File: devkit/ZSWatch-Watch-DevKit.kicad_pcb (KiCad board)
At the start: 4 copper layers, 100 x 70 mm, 129 parts, among them IC401 nPM1300-QEXX, IC501 APDS-9306-065, IC502 BMI270, IC503 LIS2MDLTR, IC504 BMP581, IC505 DRV2603RUNT, IC506 PCA9306JK, IC507 RV-8263-C8, IC601 FAN5622SX, IC602 USBLC6-2P6, IC603 MX25U51245GZ4I00, IC604 NTS0104GU12, M601 NORA-B106, Q401 PMZ550UNEYL, Q402 PMZ550UNEYL, Q403 PMZ550UNEYL, Q404 PMZB320UPEYL, X401 Battery, X402 Battery, X403 Power, X501 Current, X502 I2S, X503 Current, X504 I2C, X505 Current, X506 Current, X507 Current, X508 Current, X509 Motor, X510 Current, X601 DEBUG, X602 Current, X603 Device, X604 UART, X605 GPIO, X606 Current, X607 IO Current, X608 Display, X609 Current, X610 LED Current

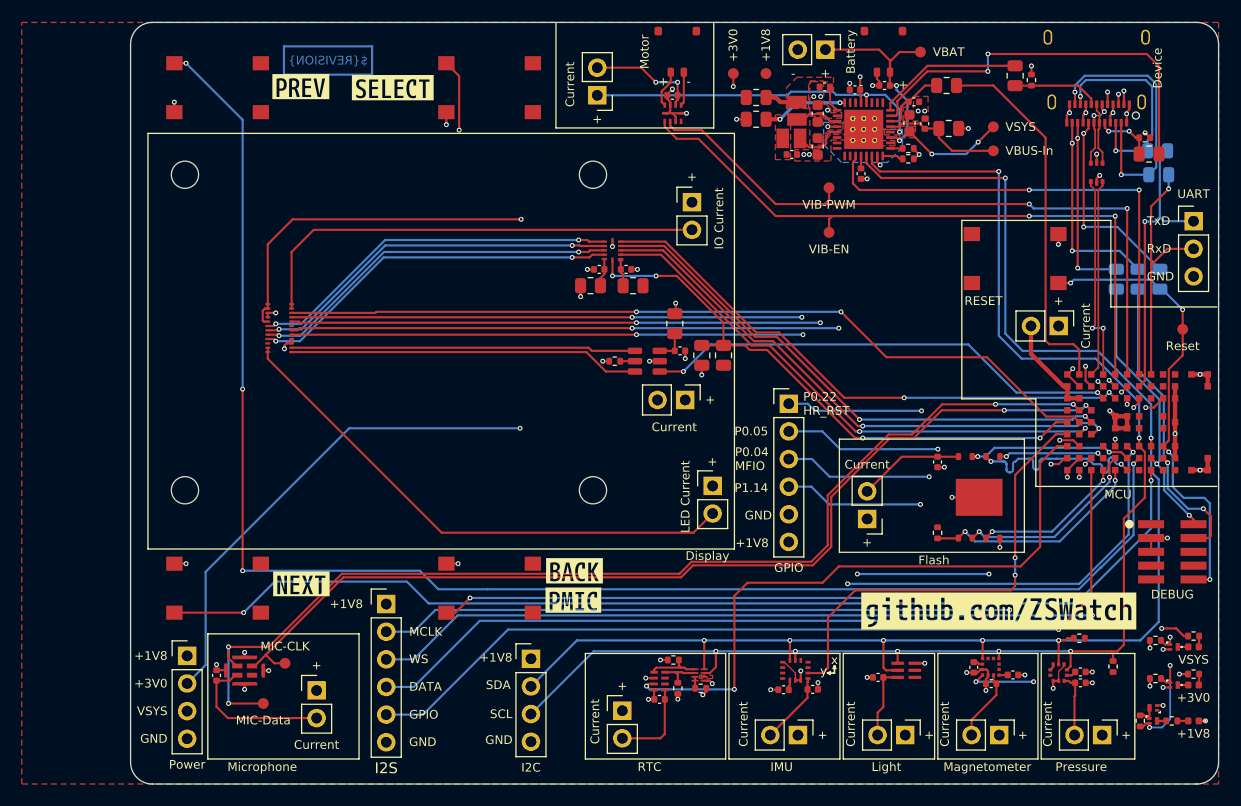
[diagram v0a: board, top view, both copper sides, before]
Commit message: Revert "Feature: Issue #180"
This reverts commit 364f4bbc8b17cbfb7f0155205af3315526997ba0.
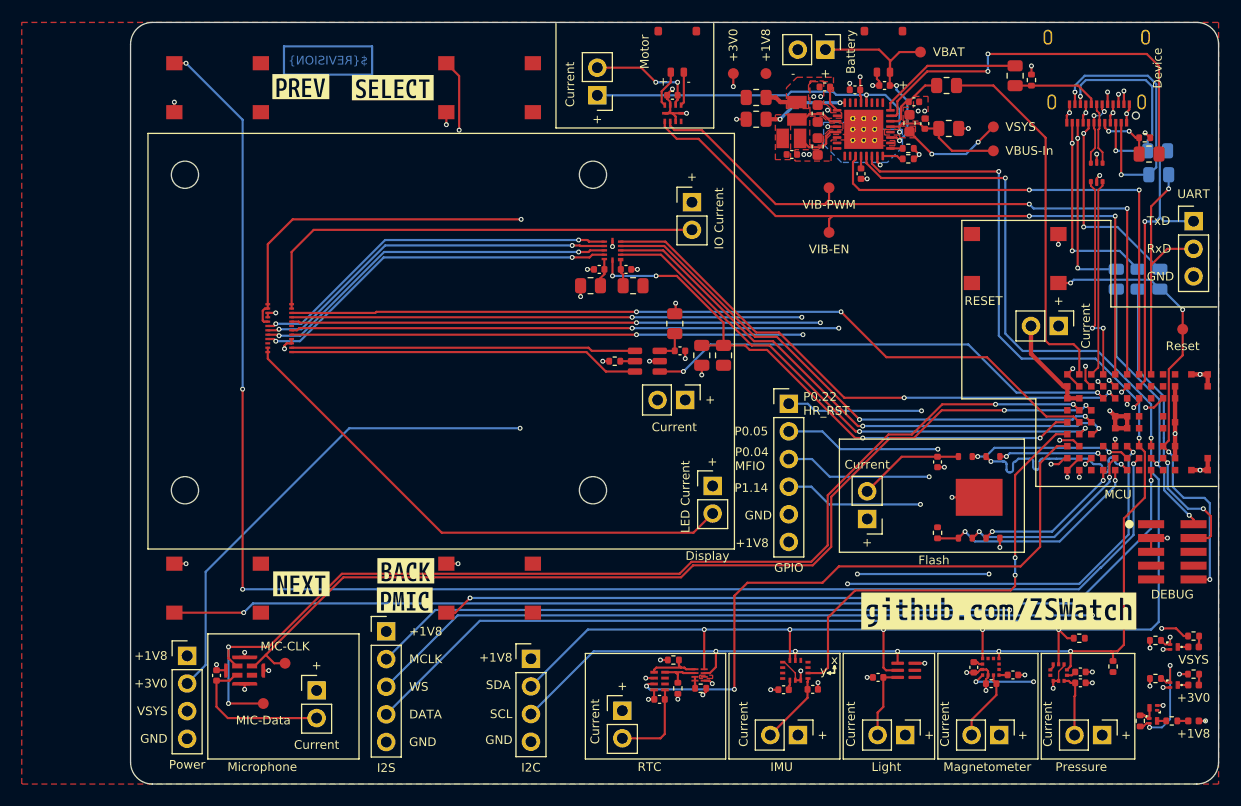
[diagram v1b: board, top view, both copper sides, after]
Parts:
- X502: footprint Connector_PinHeader_2.54mm:PinHeader_1x06_P2.54mm_Vertical -> Connector_PinHeader_2.54mm:PinHeader_1x05_P2.54mm_Vertical
- moved kibuzzard-68304289 15.5 mm to (183.3, 164.4)
- moved kibuzzard-683075F5 15.5 mm to (183.2, 167.1)
- moved X502 2.52 mm to (181.5, 170.0)
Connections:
- M601 pad C1: /Project Architecture/MCU/GPIO -> unconnected-(M601B-P0.10/TRACEDATA[1]-PadC1)
- X502 pad 5: /Project Architecture/MCU/GPIO -> GND
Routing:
- net /Project Architecture/MCU/GPIO: track 80.9 -> 0.00 mm, vias 1 -> 0
- net /Project Architecture/MCU/SDA: track 139.3 -> 144.6 mm
- net /Project Architecture/MCU/SW3: track 100.0 -> 98.3 mm
- net /Project Architecture/MCU/MCLK: track 82.1 -> 83.1 mm
- net /Project Architecture/MCU/WS: track 88.7 -> 89.8 mm
- net /Project Architecture/MCU/Data: track 91.6 -> 92.7 mm
- net /Project Architecture/MCU/SW4: track 141.8 -> 142.8 mm
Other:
- board text removed: "GPIO"

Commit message: Feature: Issue #180
- Add additional pin to I2S header

Closes #180

Signed-off-by: Daniel Kampert <DanielKampert@kampis-elektroecke.de>
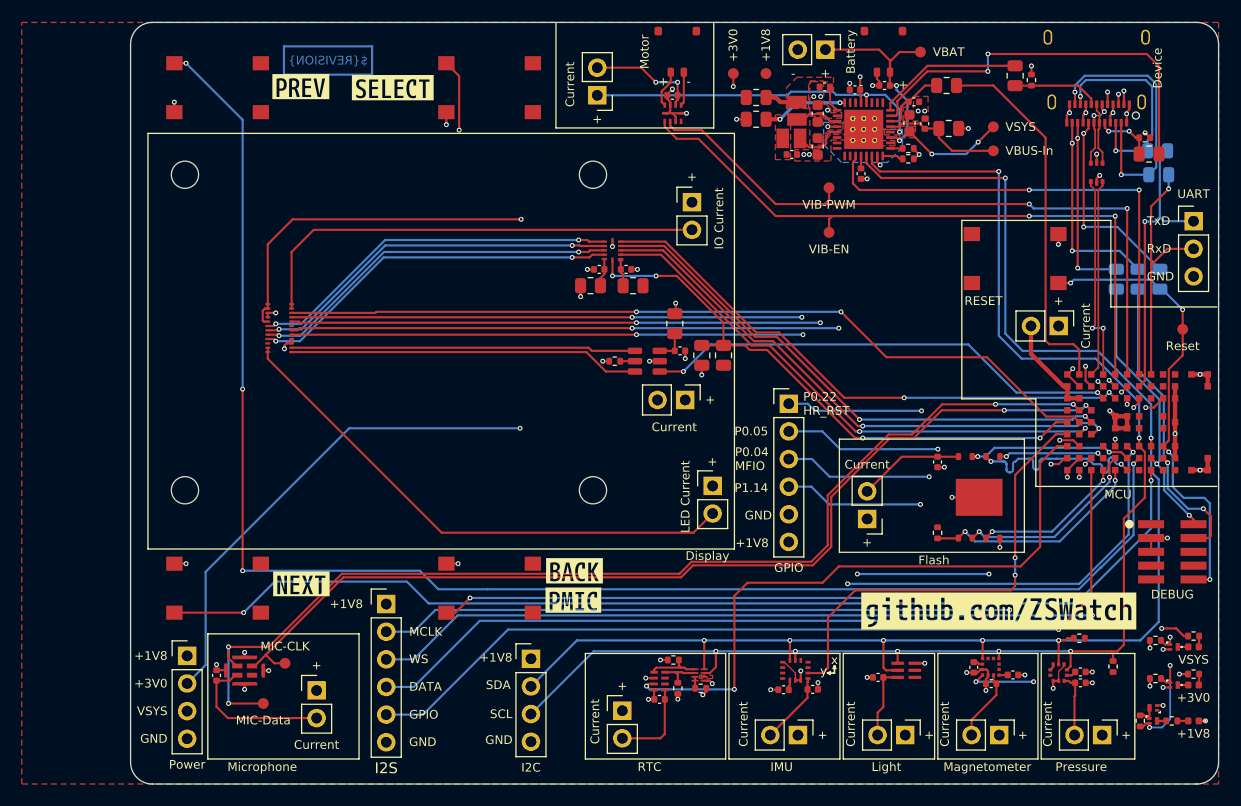
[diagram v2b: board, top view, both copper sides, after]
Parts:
- X502: footprint Connector_PinHeader_2.54mm:PinHeader_1x05_P2.54mm_Vertical -> Connector_PinHeader_2.54mm:PinHeader_1x06_P2.54mm_Vertical
- moved kibuzzard-68304289 15.5 mm to (198.8, 164.4)
- moved kibuzzard-683075F5 15.5 mm to (198.7, 167.1)
- moved X502 2.52 mm to (181.5, 167.5)
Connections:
- M601 pad C1: unconnected-(M601B-P0.10/TRACEDATA[1]-PadC1) -> /Project Architecture/MCU/GPIO
- X502 pad 5: GND -> /Project Architecture/MCU/GPIO
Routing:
- net /Project Architecture/MCU/GPIO: track 0.00 -> 80.9 mm, vias 0 -> 1
- net /Project Architecture/MCU/SDA: track 144.6 -> 139.3 mm
- net /Project Architecture/MCU/SW3: track 98.3 -> 100.0 mm
- net /Project Architecture/MCU/MCLK: track 83.1 -> 82.1 mm
- net /Project Architecture/MCU/WS: track 89.8 -> 88.7 mm
- net /Project Architecture/MCU/Data: track 92.7 -> 91.6 mm
- net /Project Architecture/MCU/SW4: track 142.8 -> 141.8 mm
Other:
- board text added: "GPIO"

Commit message: Feature: Issue #180
- Add additional header for VSYS
- Fix wrong silkscreen size for the I2S header
- Fix wrong CHANGELOG entry for issue #180

Closes #180

Signed-off-by: Daniel Kampert <DanielKampert@kampis-elektroecke.de>
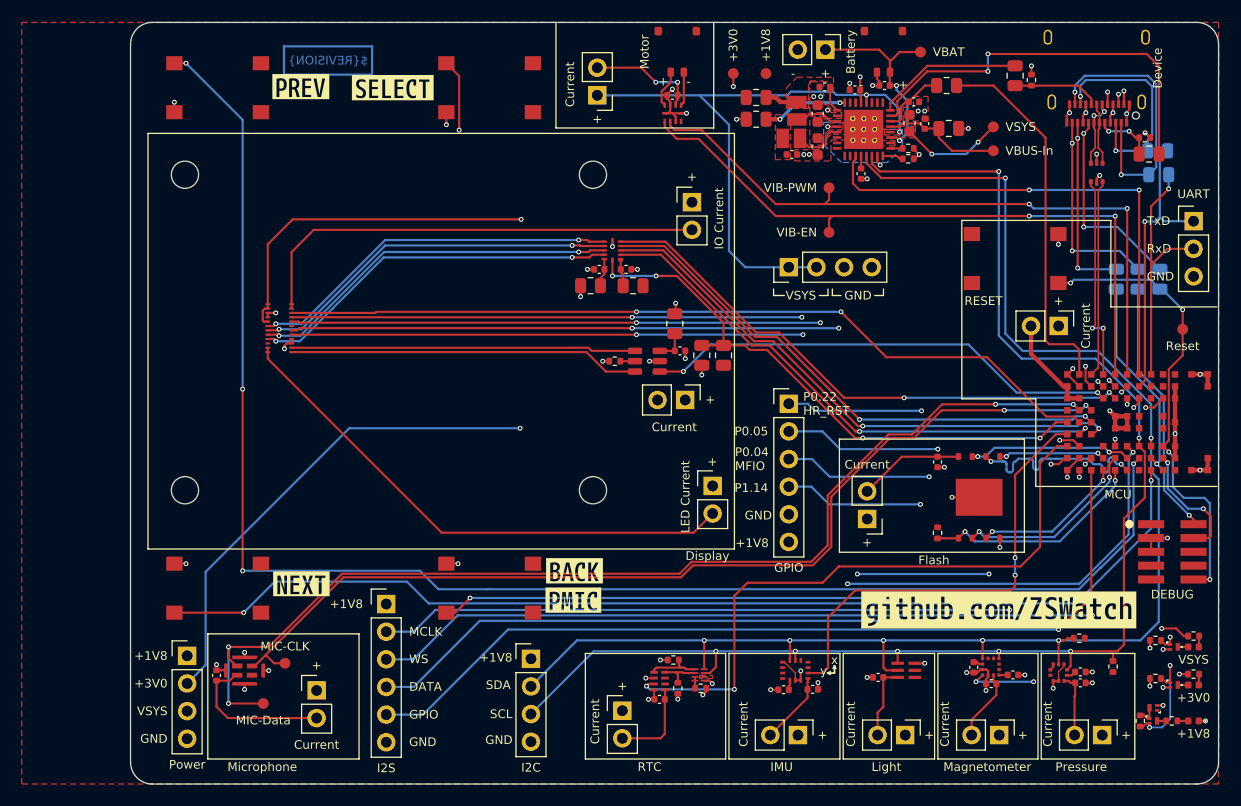
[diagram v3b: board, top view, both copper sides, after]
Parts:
- added X404: VSYS, Connector_PinHeader_2.54mm:PinHeader_1x04_P2.54mm_Vertical, F.Cu at (218.5, 136.5)
- moved kibuzzard-68303879 0.10 mm to (237.8, 168.0)
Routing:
- net /Project Architecture/Power Management/VSYS: track 200.2 -> 224.3 mm
- net /Project Architecture/MCU/SW2: track 81.2 -> 82.2 mm

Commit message: Revert "Feature: Issue #180"
This reverts commit e294da7cfd2de151837bcacc2c2eee3b2a5acfa5.
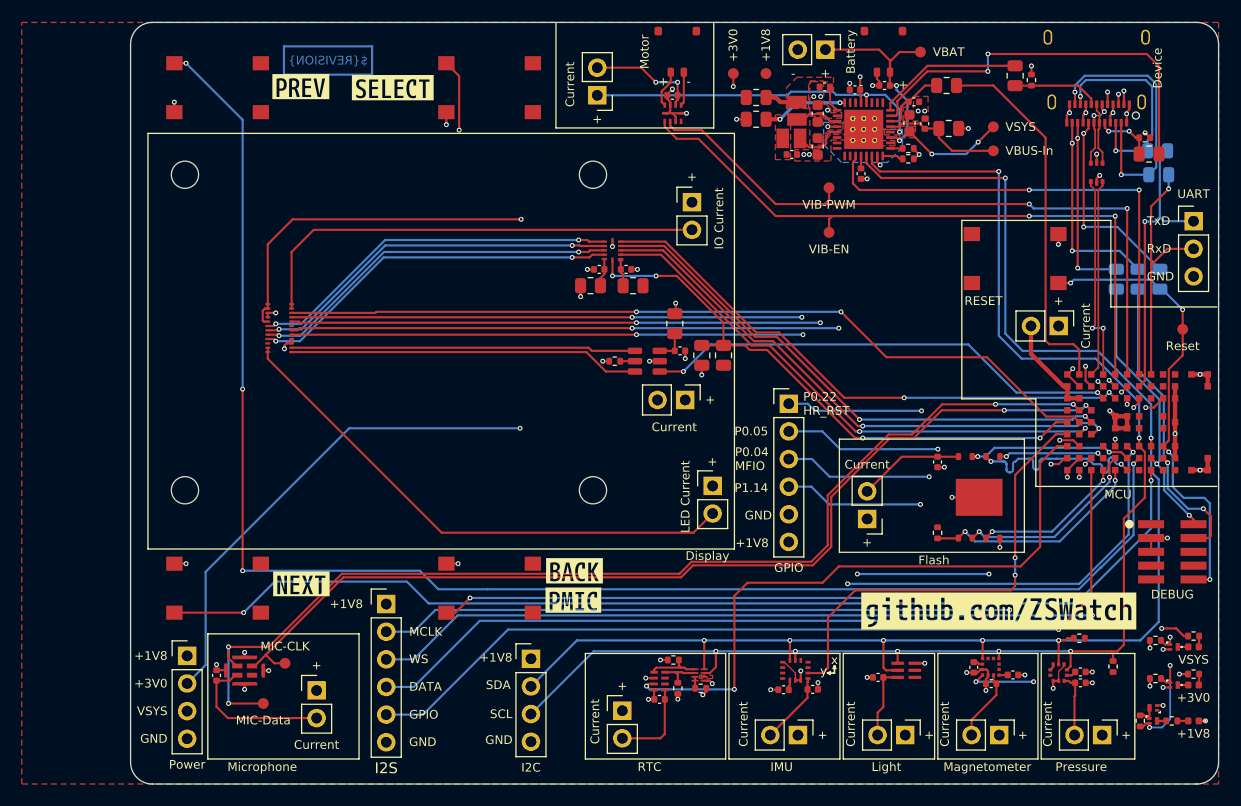
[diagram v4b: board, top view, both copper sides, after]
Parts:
- removed X404: VSYS, Connector_PinHeader_2.54mm:PinHeader_1x04_P2.54mm_Vertical
- moved kibuzzard-68303879 0.10 mm to (237.8, 168.1)
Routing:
- net /Project Architecture/Power Management/VSYS: track 224.3 -> 200.2 mm
- net /Project Architecture/MCU/SW2: track 82.2 -> 81.2 mm
